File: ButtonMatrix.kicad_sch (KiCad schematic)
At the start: 69 parts, among them SW1 SW_Push_LED, SW10 SW_Push_LED, SW11 SW_Push_LED, SW12 SW_Push_LED, SW13 SW_Push_LED, SW14 SW_Push_LED, SW15 SW_Push_LED, SW16 SW_Push_LED, SW17 SW_Push_LED, SW18 SW_Push_LED, SW19 SW_Push_LED, SW2 SW_Push_LED, SW20 SW_Push_LED, SW21 SW_Push_LED, SW22 SW_Push_LED, SW23 SW_Push_LED, SW24 SW_Push_LED, SW25 SW_Push_LED, SW26 SW_Push_LED, SW27 SW_Push_LED, SW28 SW_Push_LED, SW29 SW_Push_LED, SW3 SW_Push_LED, SW30 SW_Push_LED, SW31 SW_Push_LED, SW32 SW_Push_LED, SW33 SW_Push_LED, SW34 SW_Push_LED, SW35 SW_Push_LED, SW36 SW_Push_LED, SW37 SW_Push_LED, SW38 SW_Push_LED, SW39 SW_Push_LED, SW4 SW_Push_LED, SW40 SW_Push_LED, SW41 SW_Push_LED, SW42 SW_Push_LED, SW43 SW_Push_LED, SW44 SW_Push_LED, SW45 SW_Push_LED, SW46 SW_Push_LED, SW47 SW_Push_LED, SW48 SW_Push_LED, SW49 SW_Push_LED, SW5 SW_Push_LED, SW50 SW_Push_LED, SW51 SW_Push_LED, SW52 SW_Push_LED, SW53 SW_Push_LED, SW54 SW_Push_LED, SW55 SW_Push_LED, SW56 SW_Push_LED, SW57 SW_Push_LED, SW58 SW_Push_LED, SW59 SW_Push_LED, SW6 SW_Push_LED, SW60 SW_Push_LED, SW61 SW_Push_LED, SW62 SW_Push_LED, SW63 SW_Push_LED, SW64 SW_Push_LED, SW65 SW_Push_LED, SW66 SW_Push_LED, SW67 SW_Push_LED, SW68 SW_Push_LED, SW69 SW_Push_LED, SW7 SW_Push_LED, SW8 SW_Push_LED, SW9 SW_Push_LED

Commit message: JLCPCB rotation cleanup, kibot script fixes
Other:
- title: (none) -> Collins FMS 3000
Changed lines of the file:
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@@
   (paper "A4")
   (title_block
-    (date "%%date%%")
-    (rev "%%version%%")
+    (title "Collins FMS 3000")
+    (date "2022-11-02")
+    (rev "")
   )
   (junction (at 109.22 111.76) (diameter 0) (color 0 0 0 0)

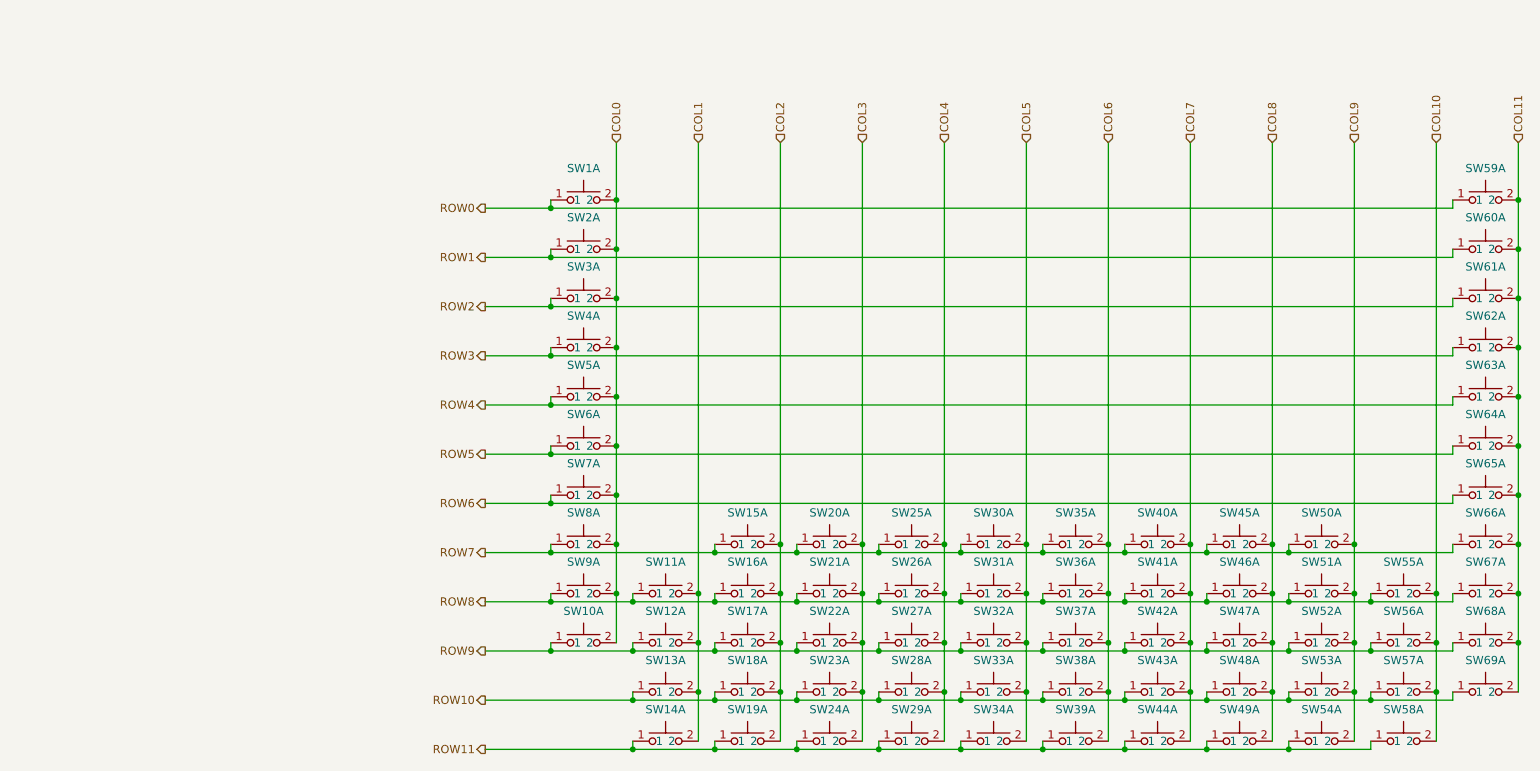
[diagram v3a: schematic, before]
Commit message: Keyboard driver (#25)
* Lots of pre-work before replacing RP2040 layout

* New RP2040 layout added

* FULLY ROUTED

* Clean up schematic

* More trace cleanup

* Final trace cleanup

Co-authored-by: Neil Enns <{ID}+{username}@users.noreply.github.com>
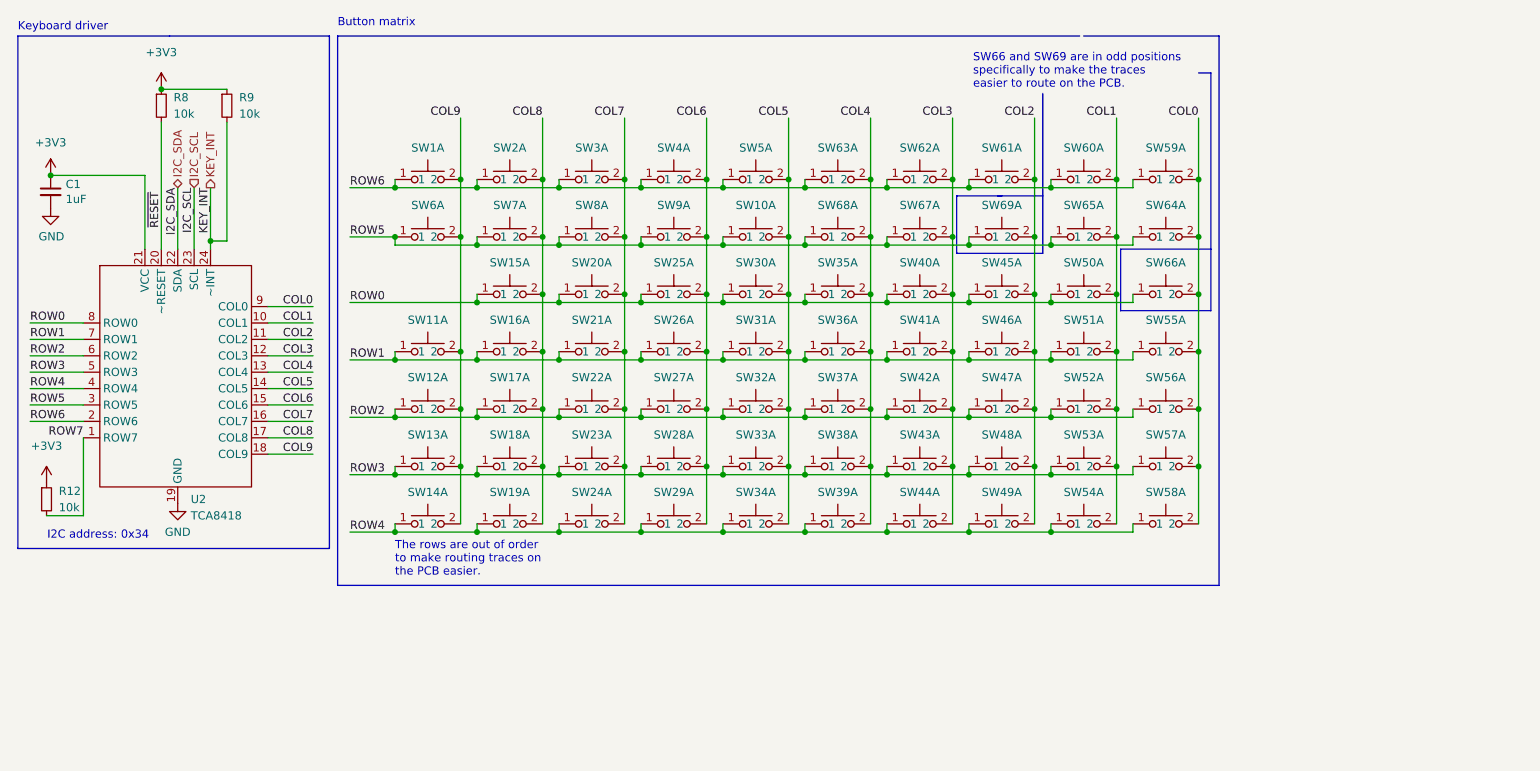
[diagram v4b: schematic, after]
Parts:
- added C1: 1uF, Custom_Footprints:Perfect_0402, symbol Device:C_Small
- added R12, R8, R9: 10k, Custom_Footprints:Perfect_0402, symbol Device:R_Small
- added U2: TCA8418, Package_DFN_QFN:WQFN-24-1EP_4x4mm_P0.5mm_EP2.6x2.6mm, symbol Custom_Symbols:TCA8418
- SW1, SW10, SW11, SW12, SW13, SW14, SW15, SW16, SW17, SW18, SW19, SW2, SW20, SW21, SW22, SW23, SW24, SW25, SW26, SW27, SW28, SW29, SW3, SW30, SW31, SW32, SW33, SW34, SW35, SW36, SW37, SW38, SW39, SW4, SW40, SW41, SW42, SW43, SW44, SW45, SW46, SW47, SW48, SW49, SW5, SW50, SW51, SW52, SW53, SW54, SW55, SW56, SW57, SW58, SW59, SW6, SW60, SW61, SW62, SW63, SW64, SW65, SW67, SW68, SW7, SW8, SW9: footprint Collins-FMS-3000:SW_PUSH_6mm -> Custom_Footprints:SW_PUSH_LED_THT
- SW66: renamed from SW69; footprint Collins-FMS-3000:SW_PUSH_6mm -> Custom_Footprints:SW_PUSH_LED_THT
- SW69: renamed from SW66; footprint Collins-FMS-3000:SW_PUSH_6mm -> Custom_Footprints:SW_PUSH_LED_THT
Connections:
- net COL10 is gone; now on net COL0: SW55.2, SW56.2, SW57.2, SW58.2
- net ROW11 is gone; now on net ROW4: SW14.1, SW19.1, SW24.1, SW29.1, SW34.1, SW39.1, SW44.1, SW49.1, SW54.1, SW58.1
- net COL0: now also SW59.2, SW64.2, SW66.2, U2.9 (COL0); no longer SW1.2, SW10.2, SW2.2, SW3.2, SW4.2, SW5.2, SW6.2, SW7.2, SW8.2, SW9.2
- net COL1: now also SW50.2, SW51.2, SW52.2, SW53.2, SW54.2, SW60.2, SW65.2, U2.10 (COL1); no longer SW11.2, SW12.2, SW13.2, SW14.2
- net COL2: now also SW45.2, SW46.2, SW47.2, SW48.2, SW49.2, SW61.2, SW69.2, U2.11 (COL2); no longer SW15.2, SW16.2, SW17.2, SW18.2, SW19.2
- net COL3: now also SW40.2, SW41.2, SW42.2, SW43.2, SW44.2, SW62.2, SW67.2, U2.12 (COL3); no longer SW20.2, SW21.2, SW22.2, SW23.2, SW24.2
- net COL4: now also SW35.2, SW36.2, SW37.2, SW38.2, SW39.2, SW63.2, SW68.2, U2.13 (COL4); no longer SW25.2, SW26.2, SW27.2, SW28.2, SW29.2
- net COL5: now also SW10.2, SW5.2, U2.14 (COL5)
- net COL6: now also SW25.2, SW26.2, SW27.2, SW28.2, SW29.2, SW4.2, SW9.2, U2.15 (COL6); no longer SW35.2, SW36.2, SW37.2, SW38.2, SW39.2
- net COL7: now also SW20.2, SW21.2, SW22.2, SW23.2, SW24.2, SW3.2, SW8.2, U2.16 (COL7); no longer SW40.2, SW41.2, SW42.2, SW43.2, SW44.2
- net COL8: now also SW15.2, SW16.2, SW17.2, SW18.2, SW19.2, SW2.2, SW7.2, U2.17 (COL8); no longer SW45.2, SW46.2, SW47.2, SW48.2, SW49.2
- net COL9: now also SW1.2, SW11.2, SW12.2, SW13.2, SW14.2, SW6.2, U2.18 (COL9); no longer SW50.2, SW51.2, SW52.2, SW53.2, SW54.2
- net ROW0: now also SW15.1, SW20.1, SW25.1, SW30.1, SW35.1, SW40.1, SW45.1, SW50.1, SW66.1, U2.8 (ROW0); no longer SW1.1, SW59.1
- net ROW1: now also SW11.1, SW16.1, SW21.1, SW26.1, SW31.1, SW36.1, SW41.1, SW46.1, SW51.1, SW55.1, U2.7 (ROW1); no longer SW2.1, SW60.1
- net ROW2: now also SW12.1, SW17.1, SW22.1, SW27.1, SW32.1, SW37.1, SW42.1, SW47.1, SW52.1, SW56.1, U2.6 (ROW2); no longer SW3.1, SW61.1
- net ROW3: now also SW13.1, SW18.1, SW23.1, SW28.1, SW33.1, SW38.1, SW43.1, SW48.1, SW53.1, SW57.1, U2.5 (ROW3); no longer SW4.1, SW62.1
- net ROW4: now also U2.4 (ROW4); no longer SW5.1, SW63.1
- net ROW5: now also SW10.1, SW65.1, SW67.1, SW68.1, SW69.1, SW7.1, SW8.1, SW9.1, U2.3 (ROW5)
- net ROW6: now also SW1.1, SW2.1, SW3.1, SW4.1, SW5.1, SW59.1, SW60.1, SW61.1, SW62.1, SW63.1, U2.2 (ROW6); no longer SW65.1, SW7.1
- net ROW7: now also R12.2, U2.1 (ROW7); no longer SW15.1, SW20.1, SW25.1, SW30.1, SW35.1, SW40.1, SW45.1, SW50.1, SW69.1, SW8.1
- removed net COL11: SW59.2, SW60.2, SW61.2, SW62.2, SW63.2, SW64.2, SW65.2, SW66.2, SW67.2, SW68.2, SW69.2
- removed net ROW10: SW13.1, SW18.1, SW23.1, SW28.1, SW33.1, SW38.1, SW43.1, SW48.1, SW53.1, SW57.1, SW66.1
- removed net ROW8: SW11.1, SW16.1, SW21.1, SW26.1, SW31.1, SW36.1, SW41.1, SW46.1, SW51.1, SW55.1, SW67.1, SW9.1
- removed net ROW9: SW10.1, SW12.1, SW17.1, SW22.1, SW27.1, SW32.1, SW37.1, SW42.1, SW47.1, SW52.1, SW56.1, SW68.1
- new net +3V3: C1.1, R12.1, R8.1, R9.1, U2.21 (VCC)
- new net GND: C1.2, U2.19 (GND)
- new net I2C_SCL: U2.23 (SCL)
- new net I2C_SDA: U2.22 (SDA)
- new net KEY_INT: R9.2, U2.24 (~INT)
- new net ~{RESET}: R8.2, U2.20 (~RESET)
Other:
- note added: "Button matrix"
- note added: "I2C address: 0x34"
- note added: "Keyboard driver"
- note added: "SW66 and SW69 are in odd positions specifically to make the traces easier to route on the PCB."
- note added: "The rows are out of order to make routing traces on the PCB easier."
- moved on the sheet: SW10A, SW11A, SW12A, SW13A, SW14A, SW15A, SW16A, SW17A, SW18A, SW19A, SW1A, SW20A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

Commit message: Renumber buttons to match key array position
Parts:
- renumbered SW66 to SW1, SW55 to SW11, SW51 to SW12, SW46 to SW13, SW41 to SW14, SW36 to SW15, SW31 to SW16, SW26 to SW17, SW21 to SW18, SW16 to SW19, SW50 to SW2, SW11 to SW20, SW56 to SW21, SW52 to SW22, SW47 to SW23, SW42 to SW24, SW37 to SW25, SW32 to SW26, SW22 to SW28, SW17 to SW29, SW45 to SW3, SW12 to SW30, SW57 to SW31, SW53 to SW32, SW48 to SW33, SW43 to SW34, SW38 to SW35, SW33 to SW36, SW28 to SW37, SW23 to SW38, SW18 to SW39, SW40 to SW4, SW13 to SW40, SW58 to SW41, SW54 to SW42, SW49 to SW43, SW39 to SW45, SW34 to SW46, SW29 to SW47, SW24 to SW48, SW19 to SW49, SW35 to SW5, SW14 to SW50, SW64 to SW51, SW65 to SW52, SW69 to SW53, SW67 to SW54, SW68 to SW55, SW10 to SW56, SW9 to SW57, SW8 to SW58, SW7 to SW59, SW30 to SW6, SW6 to SW60, SW59 to SW61, SW60 to SW62, SW61 to SW63, SW62 to SW64, SW63 to SW65, SW5 to SW66, SW4 to SW67, SW3 to SW68, SW2 to SW69, SW25 to SW7, SW1 to SW70, SW20 to SW8, SW15 to SW9
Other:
- note removed: "SW66 and SW69 are in odd positions specifically to make the traces easier to route on the PCB."
